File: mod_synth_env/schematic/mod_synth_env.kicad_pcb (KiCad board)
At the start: 2 copper layers, 29.2 x 109.2 mm, 0 parts

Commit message: Start work on envelope PCB
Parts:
- added C1: 1uF, Capacitor_THT:C_Disc_D9.0mm_W2.5mm_P5.00mm, B.Cu at (68.6, 101.6)
- added C2: 10nF, Capacitor_THT:C_Disc_D9.0mm_W2.5mm_P5.00mm, B.Cu at (135.9, 85.1)
- added D1: 1N4148, Diode_THT:D_DO-35_SOD27_P7.62mm_Horizontal, B.Cu at (172.7, 82.5)
- added D2: 1N4148, Diode_THT:D_DO-35_SOD27_P7.62mm_Horizontal, B.Cu at (134.6, 119.4)
- added D3: 1N4148, Diode_THT:D_DO-35_SOD27_P7.62mm_Horizontal, B.Cu at (108.0, 52.1)
- added D4: LED, LED_THT:LED_D5.0mm, F.Cu at (87.6, 115.6)
- added D5: 1N4148, Diode_THT:D_DO-35_SOD27_P7.62mm_Horizontal, B.Cu at (156.2, 92.7)
- added D6: 1N4148, Diode_THT:D_DO-35_SOD27_P7.62mm_Horizontal, B.Cu at (92.7, 87.6)
- added D7: 1N4148, Diode_THT:D_DO-35_SOD27_P7.62mm_Horizontal, B.Cu at (85.1, 68.6)
- added J1: AudioJack2, Connector_Audio:Jack_3.5mm_QingPu_WQP-PJ398SM_Vertical_CircularHoles, F.Cu at (82.5, 44.5)
- added J2: AudioJack2, Connector_Audio:Jack_3.5mm_QingPu_WQP-PJ398SM_Vertical_CircularHoles, F.Cu at (82.5, 127.0)
- added J3: Conn_02x08_Odd_Even, Connector_IDC:IDC-Header_2x08_P2.54mm_Vertical, B.Cu at (47.0, 124.5)
- added R1: 100k, Resistor_THT:R_Axial_DIN0207_L6.3mm_D2.5mm_P10.16mm_Horizontal, B.Cu at (106.7, 108.0)
- added R2: 10k, Resistor_THT:R_Axial_DIN0207_L6.3mm_D2.5mm_P10.16mm_Horizontal, B.Cu at (106.7, 102.9)
- added R3: 47k, Resistor_THT:R_Axial_DIN0207_L6.3mm_D2.5mm_P10.16mm_Horizontal, B.Cu at (106.7, 95.2)
- added R4: 1k, Resistor_THT:R_Axial_DIN0207_L6.3mm_D2.5mm_P10.16mm_Horizontal, B.Cu at (144.8, 119.4)
- added R5: R100k, Resistor_THT:R_Axial_DIN0207_L6.3mm_D2.5mm_P10.16mm_Horizontal, B.Cu at (149.3, 66.5)
- added R6: 1k, Resistor_THT:R_Axial_DIN0207_L6.3mm_D2.5mm_P10.16mm_Horizontal, B.Cu at (144.8, 108.0)
- added R7: 100k, Resistor_THT:R_Axial_DIN0207_L6.3mm_D2.5mm_P10.16mm_Horizontal, B.Cu at (123.8, 51.1)
- added R8: 47k, Resistor_THT:R_Axial_DIN0207_L6.3mm_D2.5mm_P10.16mm_Horizontal, B.Cu at (154.9, 100.3)
- added R9: 100k, Resistor_THT:R_Axial_DIN0207_L6.3mm_D2.5mm_P10.16mm_Horizontal, B.Cu at (136.0, 65.5)
- added RV1: 1M, Potentiometer_THT:Potentiometer_Alpha_RD901F-40-00D_Single_Vertical_CircularHoles, F.Cu at (86.4, 83.8)
- added RV2: 1M, Potentiometer_THT:Potentiometer_Alpha_RD901F-40-00D_Single_Vertical_CircularHoles, F.Cu at (86.4, 64.8)
- added SW1: SW_Push, Connector_PinHeader_1.00mm:PinHeader_1x02_P1.00mm_Vertical, B.Cu at (101.6, 87.6)
- added SW2: SW_SPDT, Connector_PinHeader_1.00mm:PinHeader_1x03_P1.00mm_Vertical, B.Cu at (115.6, 39.4)
- added U1: TL072, Package_DIP:DIP-8_W7.62mm_Socket_LongPads, B.Cu at (92.7, 100.3)
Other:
- board size 29.2 x 109.2 mm -> 59.7 x 109.2 mm

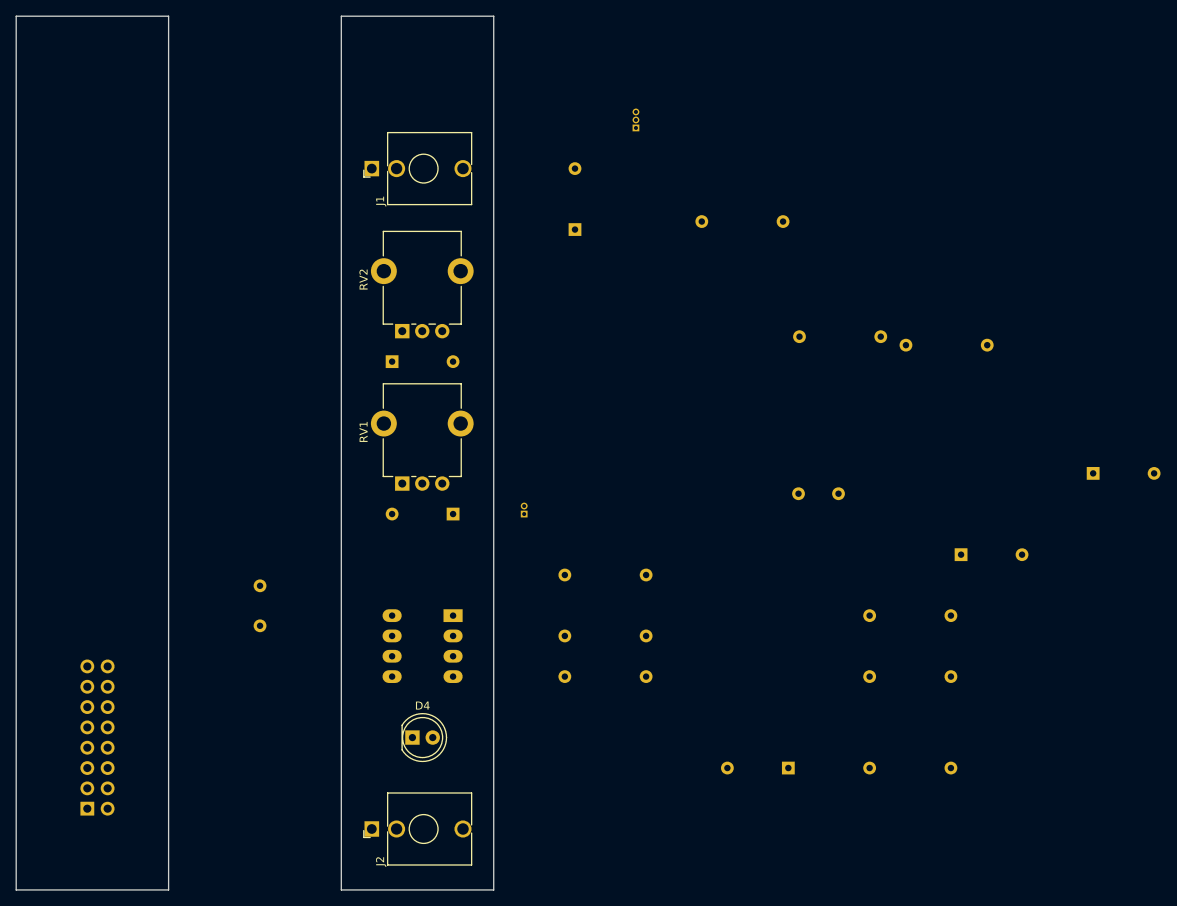
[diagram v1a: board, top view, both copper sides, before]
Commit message: Add dual pcb for envelope
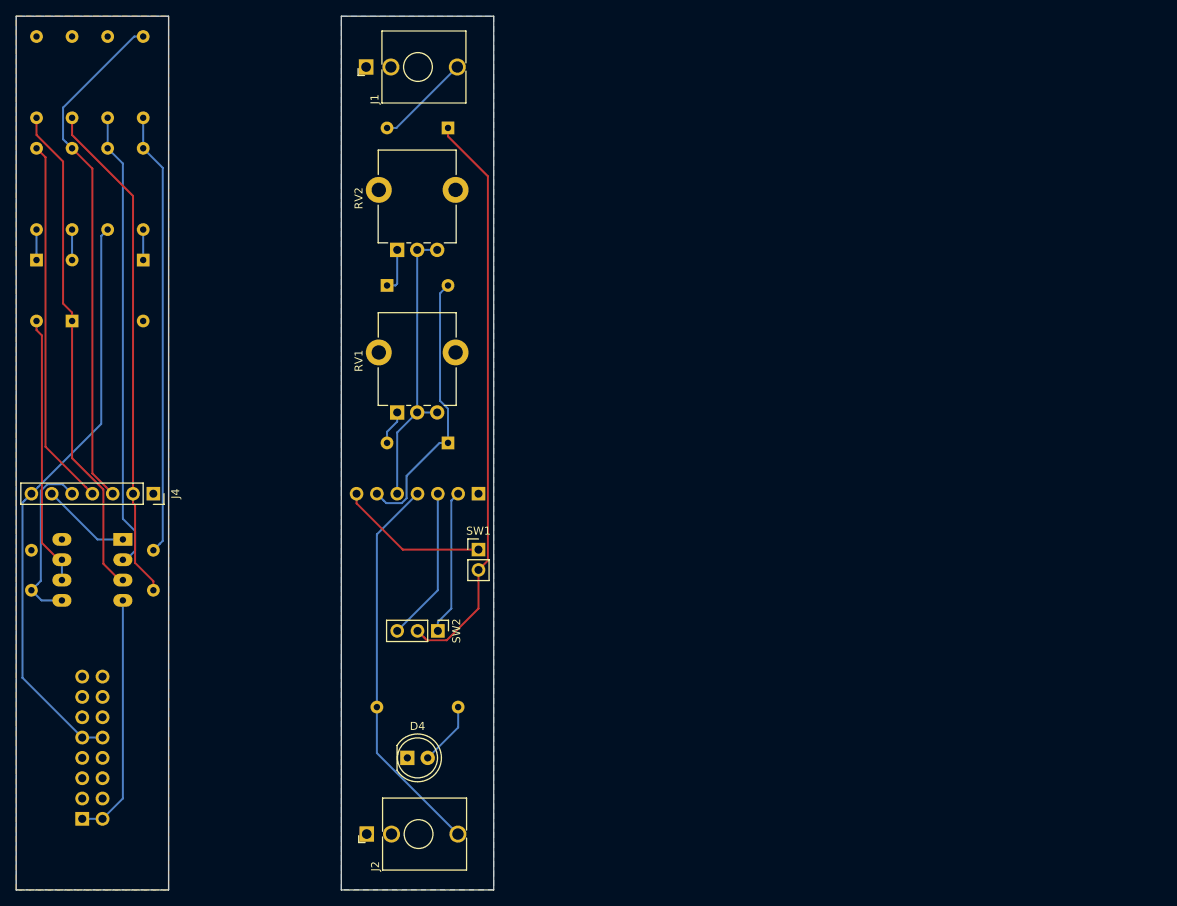
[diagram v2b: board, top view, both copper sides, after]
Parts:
- added J4: Conn_01x07_Female, Connector_PinSocket_2.54mm:PinSocket_1x07_P2.54mm_Vertical, F.Cu at (55.2, 85.1)
- added J5: Conn_01x07_Male, Connector_PinHeader_2.54mm:PinHeader_1x07_P2.54mm_Vertical, B.Cu at (95.9, 85.1)
- SW1: footprint Connector_PinHeader_1.00mm:PinHeader_1x02_P1.00mm_Vertical -> Connector_PinHeader_2.54mm:PinHeader_1x02_P2.54mm_Vertical; moved to F.Cu
- SW2: footprint Connector_PinHeader_1.00mm:PinHeader_1x03_P1.00mm_Vertical -> Connector_PinHeader_2.54mm:PinHeader_1x03_P2.54mm_Vertical; moved to F.Cu
- moved D1 129.0 mm to (45.1, 63.5), turned to 90 degrees
- moved R4 124.0 mm to (40.6, 52.1), turned to 90 degrees
- moved D2 113.4 mm to (40.6, 55.9), turned to 270 degrees
- moved R8 111.9 mm to (54.0, 52.1), turned to 90 degrees
- moved D5 108.7 mm to (54.0, 55.9), turned to 270 degrees
- moved R5 107.1 mm to (45.1, 41.9), turned to 270 degrees
- moved R1 96.1 mm to (40.6, 38.1), turned to 90 degrees
- moved R9 95.0 mm to (45.1, 38.1), turned to 90 degrees
- moved R2 86.4 mm to (49.5, 38.1), turned to 90 degrees
- moved C2 81.5 mm to (55.2, 97.2), turned to 90 degrees
- moved R3 78.2 mm to (49.5, 41.9), turned to 270 degrees
- moved R7 71.0 mm to (54.0, 38.1), turned to 90 degrees
- moved SW2 67.6 mm to (90.8, 102.2), turned to 270 degrees
- moved R6 51.6 mm to (93.3, 111.8), turned to 180 degrees
- moved U1 42.4 mm to (51.4, 90.8)
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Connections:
- C1 pad 1: Net-(C1-Pad1) -> /AMP_B_IN_PCB_A
- C2 pad 1: Net-(C2-Pad1) -> /TRIG_IN_PCB_A
- D4 pad 1: GND -> /GND_PCB_B
- D6 pad 1: Net-(D6-Pad1) -> /AMP_A_OUT_PCB_B
- D7 pad 2: Net-(D6-Pad1) -> /AMP_A_OUT_PCB_B
- J1 pad S: GND -> /GND_PCB_B
- J2 pad S: GND -> /GND_PCB_B
- J2 pad T: Net-(J2-PadT) -> /AMP_B_OUT_PCB_B
- R4 pad 2: Net-(J2-PadT) -> /AMP_B_OUT_PCB_A
- R5 pad 1: Net-(R5-Pad1) -> /GATE_IN_PCB_A
- R6 pad 2: Net-(J2-PadT) -> /AMP_B_OUT_PCB_B
- R7 pad 2: Net-(R5-Pad1) -> /GATE_IN_PCB_A
- R9 pad 1: Net-(C2-Pad1) -> /TRIG_IN_PCB_A
- RV1 pad 2: Net-(C1-Pad1) -> /AMP_B_IN_PCB_B
- RV1 pad 3: Net-(C1-Pad1) -> /AMP_B_IN_PCB_B
- RV2 pad 2: Net-(C1-Pad1) -> /AMP_B_IN_PCB_B
- RV2 pad 3: Net-(C1-Pad1) -> /AMP_B_IN_PCB_B
- SW1 pad 1: +12V -> /+12_PCB_B
- SW2 pad 1: Net-(C2-Pad1) -> /TRIG_IN_PCB_B
- SW2 pad 3: Net-(R5-Pad1) -> /GATE_IN_PCB_B
- U1 pad 1: Net-(D6-Pad1) -> /AMP_A_OUT_PCB_A
- U1 pad 5: Net-(C1-Pad1) -> /AMP_B_IN_PCB_A
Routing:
- net +12V: track 0.00 -> 73.5 mm
- net Net-(D3-Pad1): track 0.00 -> 72.4 mm
- net /GATE_IN_PCB_A: track 0.00 -> 64.5 mm
- net /TRIG_IN_PCB_A: track 0.00 -> 63.3 mm
- net Net-(D1-Pad1): track 0.00 -> 62.5 mm
- net Net-(R2-Pad1): track 0.00 -> 57.5 mm
- net Net-(C2-Pad2): track 0.00 -> 55.6 mm
- net /AMP_B_OUT_PCB_B: track 0.00 -> 48.8 mm
- net /AMP_B_OUT_PCB_A: track 0.00 -> 46.1 mm
- net /AMP_B_IN_PCB_B: track 0.00 -> 36.5 mm
- net /AMP_A_OUT_PCB_B: track 0.00 -> 34.6 mm
- net Net-(D2-Pad2): track 0.00 -> 33.9 mm
- net -12V: track 0.00 -> 30.9 mm
- net /AMP_B_IN_PCB_A: track 0.00 -> 22.0 mm
- net /GATE_IN_PCB_B: track 0.00 -> 19.2 mm
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- added copper zone on B.Cu, net /GND_PCB_B
- added copper zone on B.Cu, net GND
- added copper zone on F.Cu, net GND

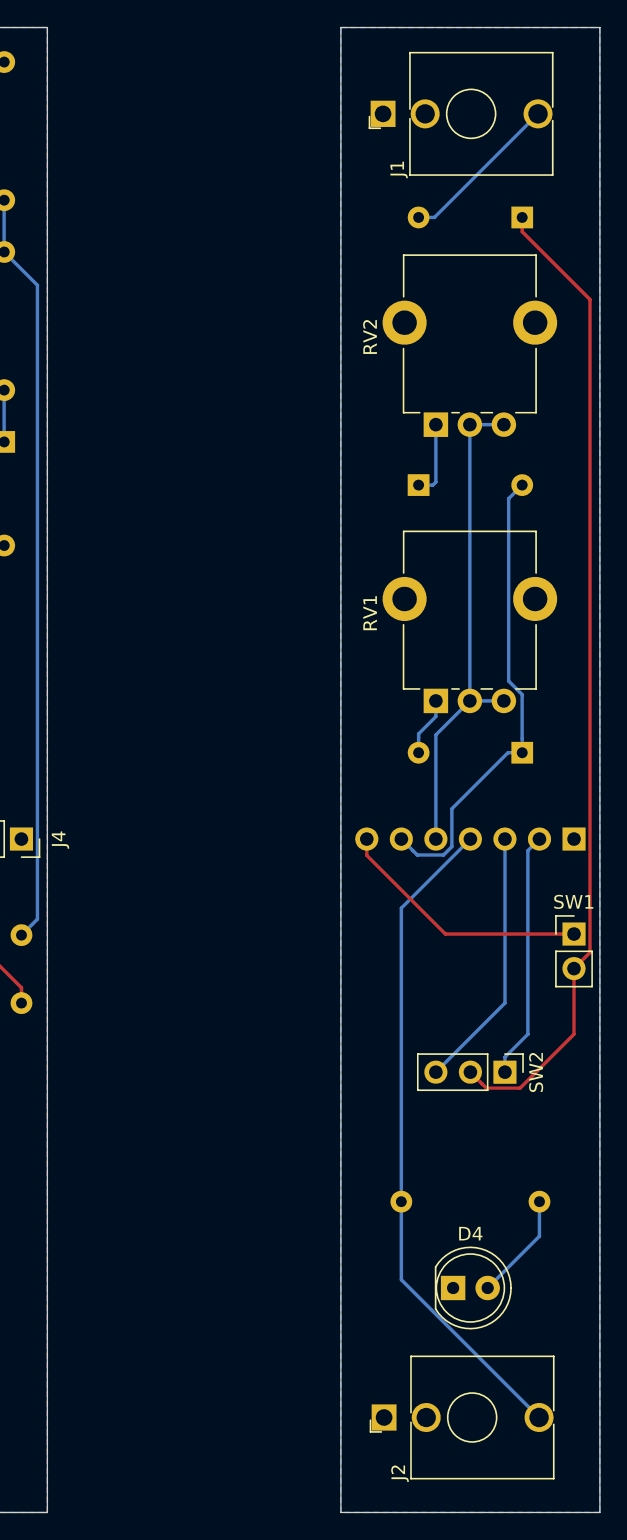
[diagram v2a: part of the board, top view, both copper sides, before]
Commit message: Move pcbs closer (0.1")
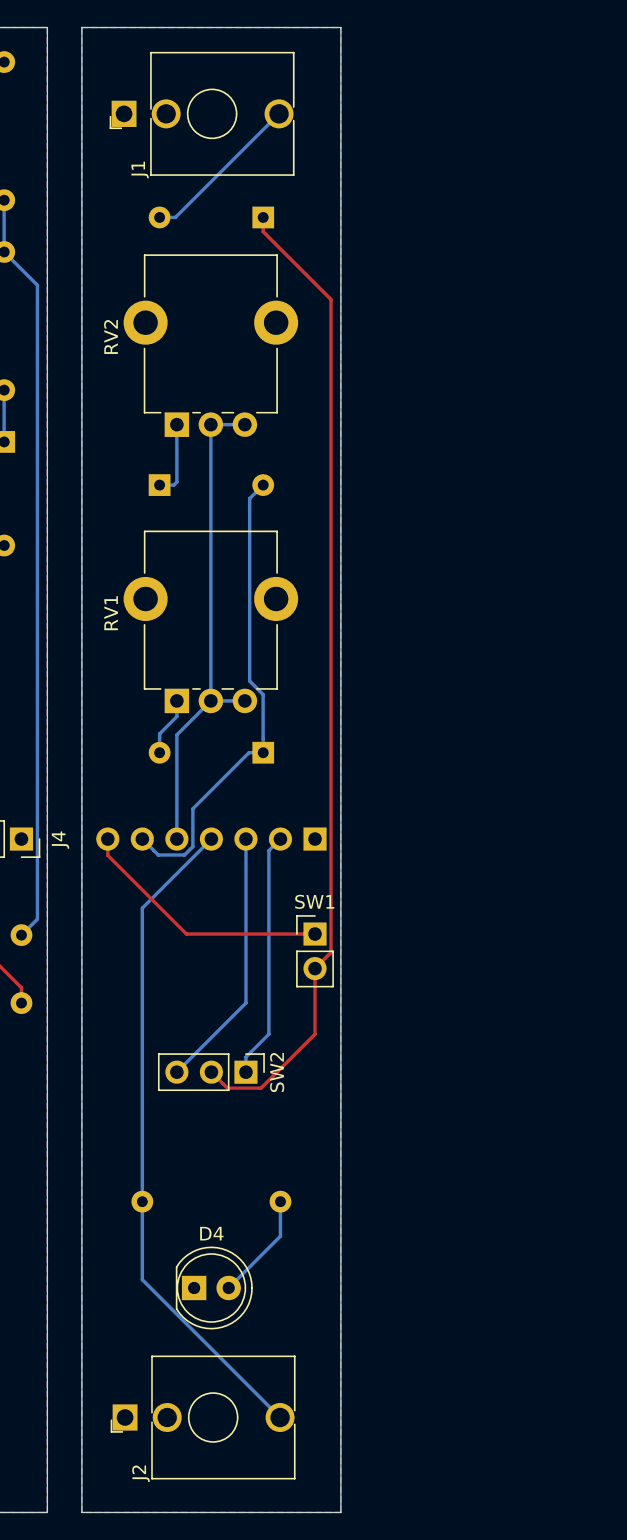
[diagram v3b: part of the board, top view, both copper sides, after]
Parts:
- moved D4 19.1 mm to (67.9, 118.1)
- moved J5 19.1 mm to (76.8, 85.1)
- moved SW1 19.1 mm to (76.8, 92.1)
- moved SW2 19.1 mm to (71.8, 102.2)
- moved J1 19.1 mm to (62.8, 31.8)
- moved J2 19.1 mm to (62.9, 127.6)
- moved D3 19.0 mm to (73.0, 39.4)
- moved D6 19.0 mm to (73.0, 78.7)
- moved D7 19.0 mm to (65.4, 59.1)
- moved R6 19.0 mm to (74.3, 111.8)
- moved RV1 19.0 mm to (66.7, 74.9)
- moved RV2 19.0 mm to (66.7, 54.6)
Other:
- board size 59.7 x 109.2 mm -> 40.6 x 109.2 mm
